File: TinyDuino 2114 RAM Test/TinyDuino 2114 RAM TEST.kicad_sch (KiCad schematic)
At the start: 11 parts, among them J1 POWER, J2 CONTROL, U1 2114, U2 74LS95, U3 74LS299, U4 74LS299

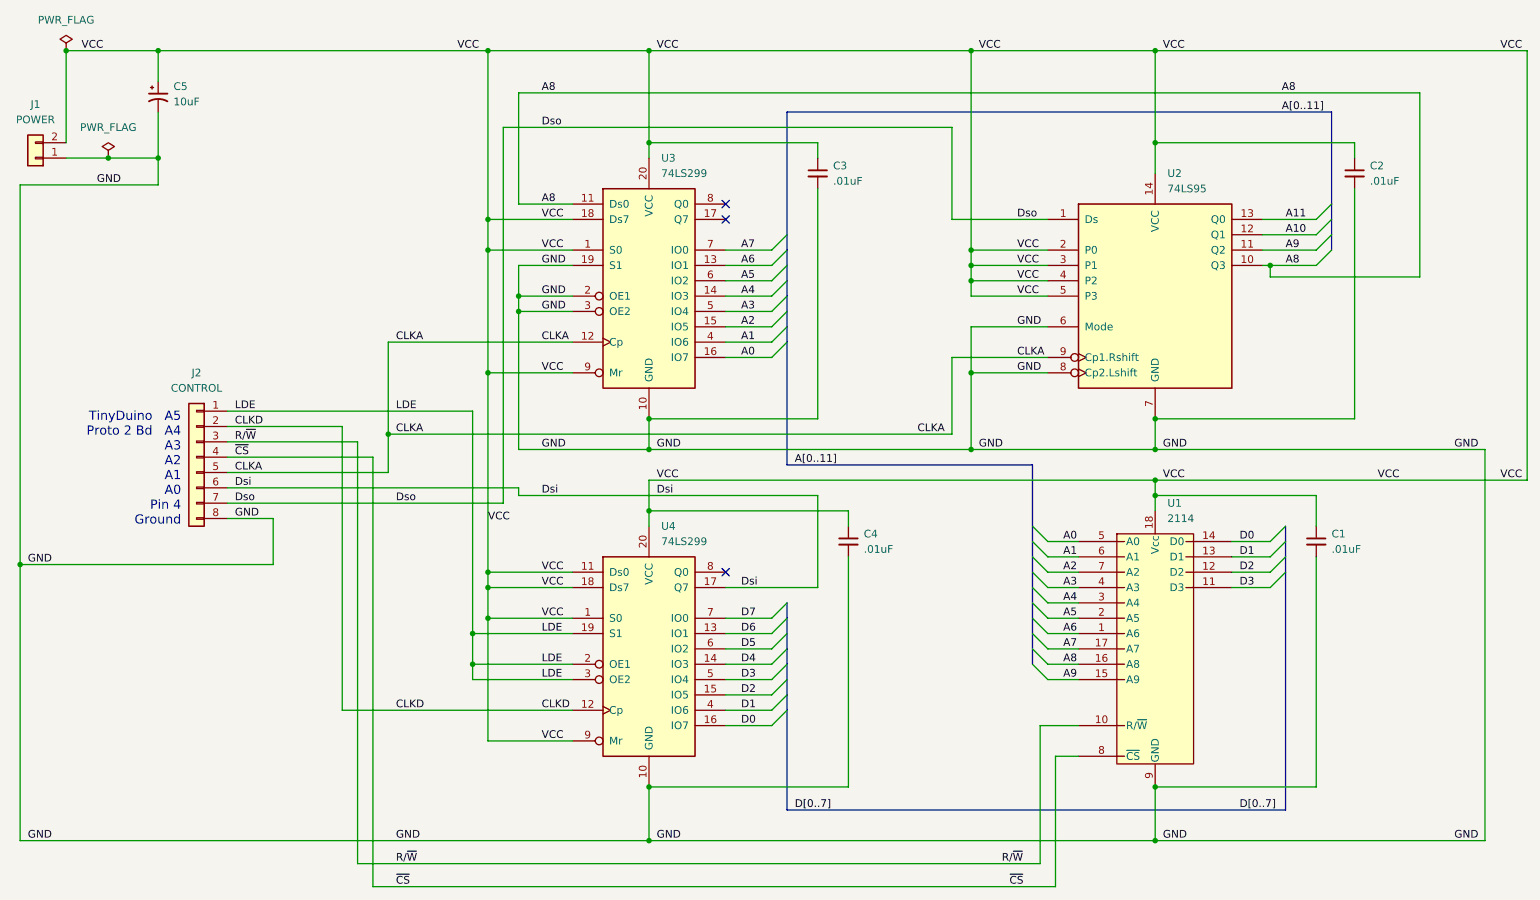
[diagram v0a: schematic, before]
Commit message: Serial line from Address Register to Data Register
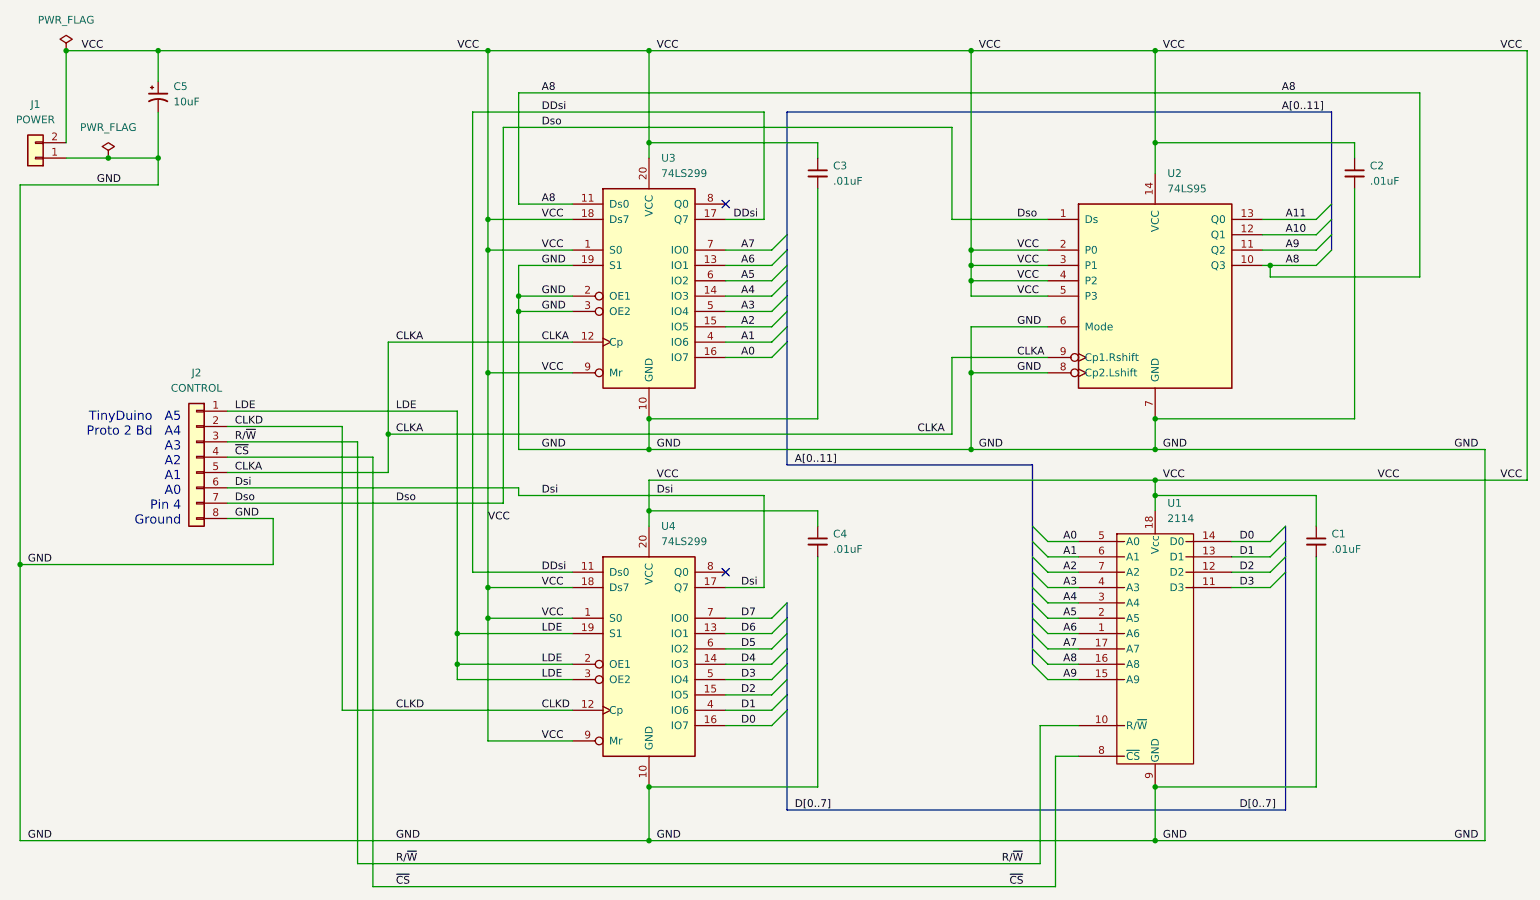
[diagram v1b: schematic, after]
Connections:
- net VCC: no longer U4.11 (Ds0)
- net DDsi: now reaches U3.17 (Q7)
- net DDsi: now also U4.11 (Ds0)
- no-connect marks 3 -> 2
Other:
- moved on the sheet: C4
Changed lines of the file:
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@@
   (title_block
     (title "TinyDuino 2114 RAM Test")
-    (date "2022-08-28")
-    (rev "1.0")
+    (date "2022-08-29")
+    (rev "1.1")
     (company "NinBra Enterprises")
     (comment 1 "Assumes 5v GPIO interface to TinyDuino")
@@
   (junction (at 175.26 22.86) (diameter 0) (color 0 0 0 0)
   )
-  (junction (at 92.71 124.46) (diameter 0) (color 0 0 0 0)
-  )
   (junction (at 40.64 40.64) (diameter 0) (color 0 0 0 0)
   )
@@
   (junction (at 175.26 60.96) (diameter 0) (color 0 0 0 0)
   )
+  (junction (at 90.17 119.38) (diameter 0) (color 0 0 0 0)
+  )
   (junction (at 121.92 99.06) (diameter 0) (color 0 0 0 0)
   )
@@
   (junction (at 121.92 38.1) (diameter 0) (color 0 0 0 0)
   )
-  (junction (at 92.71 119.38) (diameter 0) (color 0 0 0 0)
-  )
   (junction (at 205.74 144.78) (diameter 0) (color 0 0 0 0)
   )
@@
   (junction (at 100.33 66.04) (diameter 0) (color 0 0 0 0)
   )
+  (junction (at 90.17 124.46) (diameter 0) (color 0 0 0 0)
+  )
   (junction (at 205.74 83.82) (diameter 0) (color 0 0 0 0)
   )
@@
   (junction (at 121.92 88.9) (diameter 0) (color 0 0 0 0)
   )
-  (junction (at 95.25 109.22) (diameter 0) (color 0 0 0 0)
-  )
   (junction (at 95.25 76.2) (diameter 0) (color 0 0 0 0)
   )
@@
   (junction (at 40.64 22.86) (diameter 0) (color 0 0 0 0)
   )
-  (no_connect (at 134.62 50.8))
   (no_connect (at 134.62 48.26))
   (no_connect (at 134.62 109.22))
@@
     (stroke (width 0) (type default) (color 0 0 0 0))
   )
+  (wire (pts (xy 134.62 50.8) (xy 140.97 50.8))
+    (stroke (width 0) (type default) (color 0 0 0 0))
+  )
   (wire (pts (xy 40.64 45.085) (xy 40.64 40.64))
     (stroke (width 0) (type default) (color 0 0 0 0))
@@
     (stroke (width 0) (type default) (color 0 0 0 0))
   )
-  (wire (pts (xy 109.22 127) (xy 92.71 127))
+  (wire (pts (xy 109.22 127) (xy 90.17 127))
     (stroke (width 0) (type default) (color 0 0 0 0))
   )
@@
     (stroke (width 0) (type default) (color 0 0 0 0))
   )
+  (wire (pts (xy 90.17 124.46) (xy 109.22 124.46))
+    (stroke (width 0) (type default) (color 0 0 0 0))
+  )
   (wire (pts (xy 223.52 58.42) (xy 224.79 58.42))
     (stroke (width 0) (type default) (color 0 0 0 0))
@@
     (stroke (width 0) (type default) (color 0 0 0 0))
   )
-  (wire (pts (xy 92.71 124.46) (xy 92.71 127))
+  (wire (pts (xy 90.17 124.46) (xy 90.17 127))
     (stroke (width 0) (type default) (color 0 0 0 0))
   )
@@
     (stroke (width 0) (type default) (color 0 0 0 0))
   )
-  (wire (pts (xy 109.22 124.46) (xy 92.71 124.46))
-    (stroke (width 0) (type default) (color 0 0 0 0))
-  )
   (wire (pts (xy 100.33 66.04) (xy 100.33 88.9))
     (stroke (width 0) (type default) (color 0 0 0 0))
@@
     (stroke (width 0) (type default) (color 0 0 0 0))
   )
-  (wire (pts (xy 95.25 76.2) (xy 95.25 109.22))
-    (stroke (width 0) (type default) (color 0 0 0 0))
-  )
   (wire (pts (xy 40.64 22.86) (xy 95.25 22.86))
     (stroke (width 0) (type default) (color 0 0 0 0))
@@
     (stroke (width 0) (type default) (color 0 0 0 0))
   )
-  (wire (pts (xy 92.71 82.55) (xy 92.71 119.38))
+  (wire (pts (xy 90.17 82.55) (xy 90.17 119.38))
     (stroke (width 0) (type default) (color 0 0 0 0))
   )
@@
     (stroke (width 0) (type default) (color 0 0 0 0))
   )
-  (wire (pts (xy 95.25 109.22) (xy 109.22 109.22))
-    (stroke (width 0) (type default) (color 0 0 0 0))
-  )
   (wire (pts (xy 121.92 153.67) (xy 205.74 153.67))
     (stroke (width 0) (type default) (color 0 0 0 0))
@@
     (stroke (width 0) (type default) (color 0 0 0 0))
   )
+  (wire (pts (xy 140.97 50.8) (xy 140.97 33.02))
+    (stroke (width 0) (type default) (color 0 0 0 0))
+  )
   (wire (pts (xy 121.92 88.9) (xy 175.26 88.9))
     (stroke (width 0) (type default) (color 0 0 0 0))
@@
     (stroke (width 0) (type default) (color 0 0 0 0))
   )
+  (wire (pts (xy 92.71 33.02) (xy 92.71 109.22))
+    (stroke (width 0) (type default) (color 0 0 0 0))
+  )
   (wire (pts (xy 71.12 132.08) (xy 71.12 85.09))
     (stroke (width 0) (type default) (color 0 0 0 0))
@@
     (stroke (width 0) (type default) (color 0 0 0 0))
   )
-  (wire (pts (xy 52.07 82.55) (xy 92.71 82.55))
+  (wire (pts (xy 52.07 82.55) (xy 90.17 82.55))
     (stroke (width 0) (type default) (color 0 0 0 0))
   )
@@
     (stroke (width 0) (type default) (color 0 0 0 0))
   )
+  (wire (pts (xy 140.97 33.02) (xy 92.71 33.02))
+    (stroke (width 0) (type default) (color 0 0 0 0))
+  )
   (wire (pts (xy 100.33 66.04) (xy 109.22 66.04))
     (stroke (width 0) (type default) (color 0 0 0 0))
@@
     (stroke (width 0) (type default) (color 0 0 0 0))
   )
-  (wire (pts (xy 149.86 96.52) (xy 100.33 96.52))
+  (wire (pts (xy 140.97 96.52) (xy 100.33 96.52))
     (stroke (width 0) (type default) (color 0 0 0 0))
   )
@@
     (stroke (width 0) (type default) (color 0 0 0 0))
   )
-  (wire (pts (xy 92.71 124.46) (xy 92.71 119.38))
+  (wire (pts (xy 90.17 124.46) (xy 90.17 119.38))
     (stroke (width 0) (type default) (color 0 0 0 0))
   )
@@
     (stroke (width 0) (type default) (color 0 0 0 0))
   )
-  (wire (pts (xy 149.86 111.76) (xy 149.86 96.52))
+  (wire (pts (xy 140.97 111.76) (xy 140.97 96.52))
     (stroke (width 0) (type default) (color 0 0 0 0))
   )
@@
     (stroke (width 0) (type default) (color 0 0 0 0))
   )
-  (wire (pts (xy 121.92 99.06) (xy 154.94 99.06))
+  (wire (pts (xy 121.92 99.06) (xy 149.86 99.06))
     (stroke (width 0) (type default) (color 0 0 0 0))
   )
@@
     (stroke (width 0) (type default) (color 0 0 0 0))
   )
-  (wire (pts (xy 109.22 119.38) (xy 92.71 119.38))
+  (wire (pts (xy 90.17 119.38) (xy 109.22 119.38))
     (stroke (width 0) (type default) (color 0 0 0 0))
   )
@@
     (stroke (width 0) (type default) (color 0 0 0 0))
   )
-  (wire (pts (xy 154.94 101.6) (xy 154.94 99.06))
+  (wire (pts (xy 149.86 101.6) (xy 149.86 99.06))
     (stroke (width 0) (type default) (color 0 0 0 0))
   )
@@
     (stroke (width 0) (type default) (color 0 0 0 0))
   )
-  (wire (pts (xy 95.25 109.22) (xy 95.25 111.76))
+  (wire (pts (xy 95.25 76.2) (xy 95.25 111.76))
     (stroke (width 0) (type default) (color 0 0 0 0))
   )
@@
     (stroke (width 0) (type default) (color 0 0 0 0))
   )
-  (wire (pts (xy 154.94 106.68) (xy 154.94 144.78))
+  (wire (pts (xy 149.86 106.68) (xy 149.86 144.78))
     (stroke (width 0) (type default) (color 0 0 0 0))
   )
@@
     (stroke (width 0) (type default) (color 0 0 0 0))
   )
+  (wire (pts (xy 92.71 109.22) (xy 109.22 109.22))
+    (stroke (width 0) (type default) (color 0 0 0 0))
+  )
   (wire (pts (xy 59.69 107.95) (xy 17.78 107.95))
     (stroke (width 0) (type default) (color 0 0 0 0))
@@
     (stroke (width 0) (type default) (color 0 0 0 0))
   )
-  (wire (pts (xy 121.92 144.78) (xy 154.94 144.78))
+  (wire (pts (xy 121.92 144.78) (xy 149.86 144.78))
     (stroke (width 0) (type default) (color 0 0 0 0))
   )
@@
     (stroke (width 0) (type default) (color 0 0 0 0))
   )
-  (wire (pts (xy 134.62 111.76) (xy 149.86 111.76))
+  (wire (pts (xy 134.62 111.76) (xy 140.97 111.76))
     (stroke (width 0) (type default) (color 0 0 0 0))
   )
@@
     (effects (font (size 1.27 1.27)) (justify left bottom))
   )
+  (label "DDsi" (at 104.14 33.02 0)
+    (effects (font (size 1.27 1.27)) (justify left bottom))
+  )
   (label "VCC" (at 104.14 76.2 0)
     (effects (font (size 1.27 1.27)) (justify left bottom))
@@
     (effects (font (size 1.27 1.27)) (justify left bottom))
   )
+  (label "DDsi" (at 104.14 109.22 0)
+    (effects (font (size 1.27 1.27)) (justify left bottom))
+  )
   (label "VCC" (at 182.88 58.42 0)
     (effects (font (size 1.27 1.27)) (justify left bottom))
@@
     (effects (font (size 1.27 1.27)) (justify left bottom))
   )
+  (label "DDsi" (at 135.89 50.8 0)
+    (effects (font (size 1.27 1.27)) (justify left bottom))
+  )
   (label "LDE" (at 104.14 127 0)
     (effects (font (size 1.27 1.27)) (justify left bottom))
@@
   )
   (label "VCC" (at 182.88 60.96 0)
-    (effects (font (size 1.27 1.27)) (justify left bottom))
-  )
-  (label "VCC" (at 104.14 109.22 0)
     (effects (font (size 1.27 1.27)) (justify left bottom))
   )
@@
     (pin "8")
   )
-  (symbol (lib_id "Device:C_Small") (at 154.94 104.14 0) (unit 1)
+  (symbol (lib_id "Device:C_Small") (at 149.86 104.14 0) (unit 1)
     (in_bom yes) (on_board yes)
-    (property "Reference" "C4" (id 0) (at 157.48 102.8762 0)
-      (effects (font (size 1.27 1.27)) (justify left))
-    )
-    (property "Value" ".01uF" (id 1) (at 157.48 105.4162 0)
-      (effects (font (size 1.27 1.27)) (justify left))
-    )
-    (property "Footprint" "" (id 2) (at 154.94 104.14 0)
-      (effects (font (size 1.27 1.27)) hide)
-    )
-    (property "Datasheet" "~" (id 3) (at 154.94 104.14 0)
-      (effects (font (size 1.27 1.27)) hide)
-    )
+    (property "Reference" "C4" (id 0) (at 152.4 102.8762 0)
+      (effects (font (size 1.27 1.27)) (justify left))
+    )
+    (property "Value" ".01uF" (id 1) (at 152.4 105.4162 0)
+      (effects (font (size 1.27 1.27)) (justify left))
+    )
+    (property "Footprint" "" (id 2) (at 149.86 104.14 0)
+      (effects (font (size 1.27 1.27)) hide)
+    )
+    (property "Datasheet" "~" (id 3) (at 149.86 104.14 0)
+      (effects (font (size 1.27 1.27)) hide)
+    )
